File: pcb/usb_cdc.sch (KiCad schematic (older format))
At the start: 131 parts, among them J101 RS232, J102 USB, P101 I2C, P102 JATG, P103 CONN_2, P104 CONN_2, P105 CONN_2, P106 CONN_2, P107 CONN_2, Q101 BC817-40, Q102 BC817-40, Q103 MOSFET_N, Q104 MOSFET_N, Q105 MOSFET_N, Q106 MOSFET_N, Q107 MOSFET_N, Q108 MOSFET_N, Q109 MOSFET_N, Q110 MOSFET_N, Q111 MOSFET_N, Q112 MOSFET_N, Q113 MOSFET_N, Q114 MOSFET_N, Q115 MOSFET_N, Q116 MOSFET_N, Q117 MOSFET_N, Q118 MOSFET_N, U101 MAX232, U102 4001, U103 4001, U104 4001, X101 8MHz

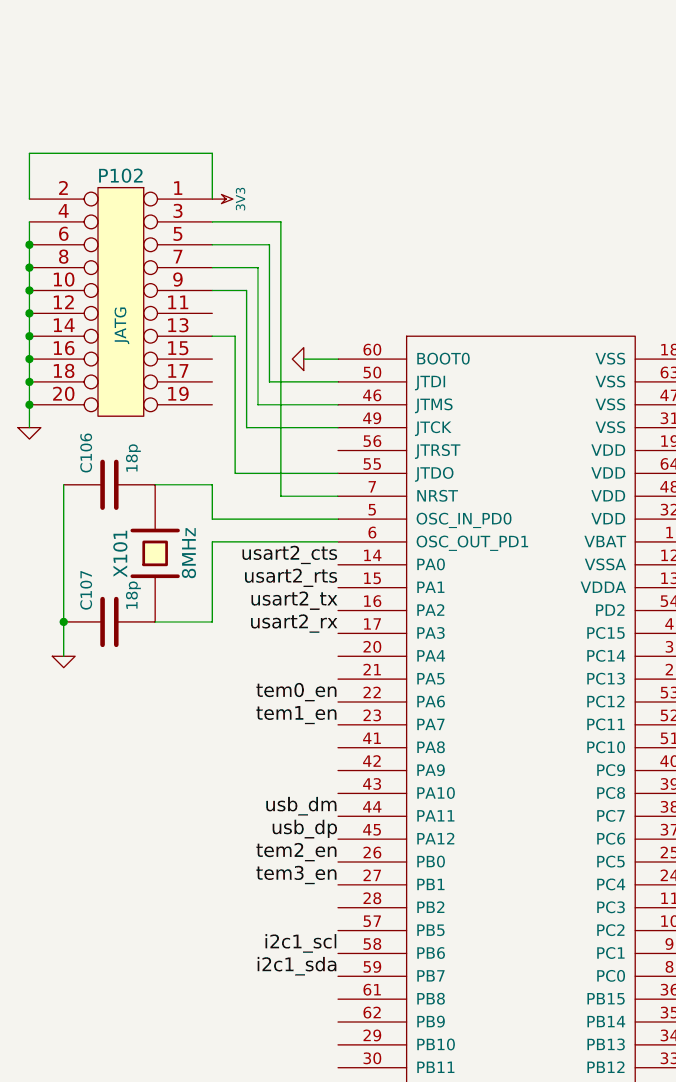
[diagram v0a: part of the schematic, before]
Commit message: implemented sensors interaction. adapt schematic for ifrmware update via uart
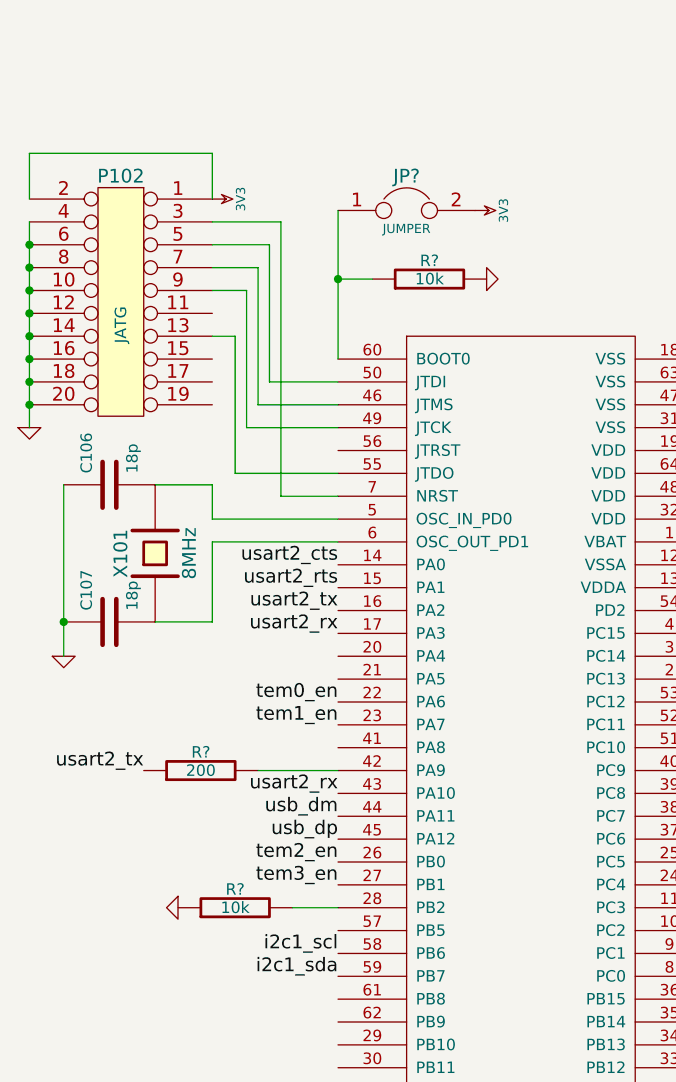
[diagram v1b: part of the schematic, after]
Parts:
- added JP?: JUMPER, symbol JUMPER
- added R? (x2): 10k, symbol R
- added R?: 200, symbol R
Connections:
- wire segments 292 -> 295
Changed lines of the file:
@@
-EESchema Schematic File Version 2  date Пнд 10 Июн 2013 18:05:02
+EESchema Schematic File Version 2  date Чтв 27 Июн 2013 16:33:48
 LIBS:power
 LIBS:device
@@
 Sheet 1 1
 Title ""
-Date "10 jun 2013"
+Date "27 jun 2013"
 Rev ""
 Comp ""
@@
 Comment4 ""
 $EndDescr
+Wire Wire Line
+	5950 4950 6300 4950
+Connection ~ 6300 2800
+Wire Wire Line
+	6450 2800 6300 2800
 Wire Notes Line
 	8000 7300 8000 7400
@@
 	8200 3550 7900 3550
 Wire Wire Line
-	6150 3150 6300 3150
-Wire Wire Line
 	5750 3950 5750 4300
 Wire Wire Line
@@
 Wire Notes Line
 	8000 8050 8000 7950
+Wire Wire Line
+	6300 3150 6300 2500
+Wire Wire Line
+	6100 5550 6300 5550
+$Comp
+L R R?
+U 1 1 51CC30F7
+P 5700 4950
+F 0 "R?" V 5780 4950 50  0000 C CNN
+F 1 "200" V 5700 4950 50  0000 C CNN
+	1    5700 4950
+	0    -1   -1   0
+$EndComp
+$Comp
+L GND #PWR?
+U 1 1 51CC2D9D
+P 5600 5550
+F 0 "#PWR?" H 5600 5550 30  0001 C CNN
+F 1 "GND" H 5600 5480 30  0001 C CNN
+	1    5600 5550
+	0    1    1    0
+$EndComp
+$Comp
+L R R?
+U 1 1 51CC2CF0
+P 5850 5550
+F 0 "R?" V 5930 5550 50  0000 C CNN
+F 1 "10k" V 5850 5550 50  0000 C CNN
+	1    5850 5550
+	0    -1   -1   0
+$EndComp
+$Comp
+L GND #PWR?
+U 1 1 51CC2CC7
+P 6950 2800
+F 0 "#PWR?" H 6950 2800 30  0001 C CNN
+F 1 "GND" H 6950 2730 30  0001 C CNN
+	1    6950 2800
+	0    -1   -1   0
+$EndComp
+$Comp
+L R R?
+U 1 1 51CC2CAD
+P 6700 2800
+F 0 "R?" V 6780 2800 50  0000 C CNN
+F 1 "10k" V 6700 2800 50  0000 C CNN
+	1    6700 2800
+	0    -1   -1   0
+$EndComp
+$Comp
+L 3V3 #PWR?
+U 1 1 51CC2C90
+P 6900 2500
+F 0 "#PWR?" H 6900 2600 40  0001 C CNN
+F 1 "3V3" H 6900 2625 40  0000 C CNN
+	1    6900 2500
+	0    1    1    0
+$EndComp
+$Comp
+L JUMPER JP?
+U 1 1 51CC2C58
+P 6600 2500
+F 0 "JP?" H 6600 2650 60  0000 C CNN
+F 1 "JUMPER" H 6600 2420 40  0000 C CNN
+	1    6600 2500
+	1    0    0    -1
+$EndComp
+Text Label 6300 5050 2    60   ~ 0
+usart2_rx
+Text Label 5450 4950 2    60   ~ 0
+usart2_tx
 Text Label 11650 11950 2    60   ~ 0
 tem3_dir
@@
 $EndComp
 $Comp
-L GND #PWR116
-U 1 1 514CAD39
-P 6150 3150
-F 0 "#PWR116" H 6150 3150 30  0001 C CNN
-F 1 "GND" H 6150 3080 30  0001 C CNN
-	1    6150 3150
-	0    1    -1   0
-$EndComp
-$Comp

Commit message: schematic: add limit switches inputs, usb led, system led, optocouplers resistors, usart2_rx protective resistor
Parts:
- added D? (x2): LED, symbol LED
- added P?: CONN_6, symbol CONN_6
- added R?: 200, symbol R
- added R? (x2): 1k, symbol R
- added R? (x8): R, symbol R
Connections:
- net labels added: ls_0, ls_1, ls_2, ls_3, ls_4
- wire segments 295 -> 306
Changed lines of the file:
@@
-EESchema Schematic File Version 2  date Чтв 27 Июн 2013 16:33:48
+EESchema Schematic File Version 2  date Втр 30 Июл 2013 22:41:59
 LIBS:power
 LIBS:device
@@
 Sheet 1 1
 Title ""
-Date "27 jun 2013"
+Date "30 jul 2013"
 Rev ""
 Comp ""
@@
 Comment4 ""
 $EndDescr
+$Comp
+L R R?
+U 1 1 51F808E6
+P 11400 12650
+F 0 "R?" V 11480 12650 50  0000 C CNN
+F 1 "R" V 11400 12650 50  0000 C CNN
+	1    11400 12650
+	0    -1   -1   0
+$EndComp
+$Comp
+L R R?
+U 1 1 51F808E1
+P 11400 11950
+F 0 "R?" V 11480 11950 50  0000 C CNN
+F 1 "R" V 11400 11950 50  0000 C CNN
+	1    11400 11950
+	0    -1   -1   0
+$EndComp
+$Comp
+L R R?
+U 1 1 51F808CA
+P 11400 10300
+F 0 "R?" V 11480 10300 50  0000 C CNN
+F 1 "R" V 11400 10300 50  0000 C CNN
+	1    11400 10300
+	0    -1   -1   0
+$EndComp
+$Comp
+L R R?
+U 1 1 51F808BE
+P 11400 9600
+F 0 "R?" V 11480 9600 50  0000 C CNN
+F 1 "R" V 11400 9600 50  0000 C CNN
+	1    11400 9600
+	0    -1   -1   0
+$EndComp
+$Comp
+L R R?
+U 1 1 51F808A7
+P 11400 7950
+F 0 "R?" V 11480 7950 50  0000 C CNN
+F 1 "R" V 11400 7950 50  0000 C CNN
+	1    11400 7950
+	0    -1   -1   0
+$EndComp
+$Comp
+L R R?
+U 1 1 51F8089B
+P 11400 7250
+F 0 "R?" V 11480 7250 50  0000 C CNN
+F 1 "R" V 11400 7250 50  0000 C CNN
+	1    11400 7250
+	0    -1   -1   0
+$EndComp
+$Comp
+L R R?
+U 1 1 51F8088A
+P 11400 5600
+F 0 "R?" V 11480 5600 50  0000 C CNN
+F 1 "R" V 11400 5600 50  0000 C CNN
+	1    11400 5600
+	0    -1   -1   0
+$EndComp
+$Comp
+L R R?
+U 1 1 51F80878
+P 11400 4900
+F 0 "R?" V 11480 4900 50  0000 C CNN
+F 1 "R" V 11400 4900 50  0000 C CNN
+	1    11400 4900
+	0    -1   -1   0
+$EndComp
+Wire Wire Line
+	9350 4650 9450 4650
+Wire Wire Line
+	9450 4650 9450 4750
+Wire Wire Line
+	5850 7600 6100 7600
+Wire Wire Line
+	5950 5050 6300 5050
 Wire Wire Line
 	5950 4950 6300 4950
@@
 Wire Wire Line
 	6100 5550 6300 5550
+Wire Wire Line
+	9300 5700 9300 5600
+Wire Wire Line
+	9300 5600 9350 5600
+Wire Wire Line
+	5350 7700 5350 7600
+Wire Wire Line
+	5350 7600 5450 7600
+Wire Wire Line
+	7900 4350 8300 4350
+Wire Wire Line
+	8300 4350 8300 4650
+Wire Wire Line
+	8300 4650 8450 4650
+$Comp
+L GND #PWR?
+U 1 1 51F80817
+P 9450 4750
+F 0 "#PWR?" H 9450 4750 30  0001 C CNN
+F 1 "GND" H 9450 4680 30  0001 C CNN
+	1    9450 4750
+	1    0    0    -1
+$EndComp
+$Comp
+L R R?
+U 1 1 51F80802
+P 8700 4650
+F 0 "R?" V 8780 4650 50  0000 C CNN
+F 1 "1k" V 8700 4650 50  0000 C CNN
+	1    8700 4650
+	0    -1   -1   0
+$EndComp
+$Comp
+L LED D?
+U 1 1 51F807B1
+P 9150 4650
+F 0 "D?" H 9150 4750 50  0000 C CNN
+F 1 "LED" H 9150 4550 50  0000 C CNN
+	1    9150 4650
+	1    0    0    -1
+$EndComp
+$Comp
+L R R?
+U 1 1 51F8075A
+P 6350 7600
+F 0 "R?" V 6430 7600 50  0000 C CNN
+F 1 "1k" V 6350 7600 50  0000 C CNN
+	1    6350 7600
+	0    -1   -1   0
+$EndComp
+$Comp
+L GND #PWR?
+U 1 1 51F8074C
+P 5350 7700
+F 0 "#PWR?" H 5350 7700 30  0001 C CNN
+F 1 "GND" H 5350 7630 30  0001 C CNN
+	1    5350 7700
+	1    0    0    -1
+$EndComp
+$Comp
+L LED D?
+U 1 1 51F8073A
+P 5650 7600
+F 0 "D?" H 5650 7700 50  0000 C CNN
+F 1 "LED" H 5650 7500 50  0000 C CNN
+	1    5650 7600
+	-1   0    0    -1
+$EndComp
+$Comp
+L R R?
+U 1 1 51F806C2
+P 5700 5050
+F 0 "R?" V 5780 5050 50  0000 C CNN
+F 1 "200" V 5700 5050 50  0000 C CNN
+	1    5700 5050
+	0    -1   -1   0
+$EndComp
+Text Label 9350 5100 2    60   ~ 0
+ls_4
+$Comp
+L CONN_6 P?
+U 1 1 51F80666
+P 9700 5350
+F 0 "P?" V 9650 5350 60  0000 C CNN
+F 1 "CONN_6" V 9750 5350 60  0000 C CNN
+	1    9700 5350
+	1    0    0    -1
+$EndComp
+Text Label 7900 5050 0    60   ~ 0
+ls_4
+Text Label 9350 5200 2    60   ~ 0
+ls_3
+Text Label 9350 5300 2    60   ~ 0
+ls_2
+Text Label 9350 5400 2    60   ~ 0
+ls_1
+Text Label 9350 5500 2    60   ~ 0
+ls_0
+$Comp
+L GND #PWR?
+U 1 1 51F8058D
+P 9300 5700
+F 0 "#PWR?" H 9300 5700 30  0001 C CNN
+F 1 "GND" H 9300 5630 30  0001 C CNN
+	1    9300 5700
+	1    0    0    -1
+$EndComp
+Text Label 7900 5250 0    60   ~ 0
+ls_3
+Text Label 7900 5450 0    60   ~ 0
+ls_2
+Text Label 7900 5650 0    60   ~ 0
+ls_1
+Text Label 7900 5850 0    60   ~ 0
+ls_0
 $Comp
 L R R?
@@
 	1    0    0    -1
 $EndComp
-Text Label 6300 5050 2    60   ~ 0
+Text Label 5450 5050 2    60   ~ 0
 usart2_rx
 Text Label 5450 4950 2    60   ~ 0
 usart2_tx
-Text Label 11650 11950 2    60   ~ 0
+Text Label 11150 11950 2    60   ~ 0
 tem3_dir
-Text Label 11650 12650 2    60   ~ 0
+Text Label 11150 12650 2    60   ~ 0
 tem3_en
-Text Label 11650 9600 2    60   ~ 0
+Text Label 11150 9600 2    60   ~ 0
 tem2_dir
-Text Label 11650 10300 2    60   ~ 0
+Text Label 11150 10300 2    60   ~ 0
 tem2_en
-Text Label 11650 7250 2    60   ~ 0
+Text Label 11150 7250 2    60   ~ 0
 tem1_dir
-Text Label 11650 7950 2    60   ~ 0
+Text Label 11150 7950 2    60   ~ 0
 tem1_en
-Text Label 11650 5600 2    60   ~ 0
+Text Label 11150 5600 2    60   ~ 0
 tem0_en
-Text Label 11650 4900 2    60   ~ 0
+Text Label 11150 4900 2    60   ~ 0
 tem0_dir
 $Comp

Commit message: schematic: moar LEDs
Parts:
- removed P?: CONN_6, symbol CONN_6
- added D? (x4): LED, symbol LED
- added P?: CONN_5X2, symbol CONN_5X2
- added R? (x4): 1k, symbol R
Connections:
- wire segments 306 -> 313
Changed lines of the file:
@@
-EESchema Schematic File Version 2  date Втр 30 Июл 2013 22:41:59
+EESchema Schematic File Version 2  date Срд 31 Июл 2013 16:10:16
 LIBS:power
 LIBS:device
@@
 Sheet 1 1
 Title ""
-Date "30 jul 2013"
+Date "31 jul 2013"
 Rev ""
 Comp ""
@@
 Comment4 ""
 $EndDescr
-$Comp
-L R R?
-U 1 1 51F808E6
-P 11400 12650
-F 0 "R?" V 11480 12650 50  0000 C CNN
-F 1 "R" V 11400 12650 50  0000 C CNN
-	1    11400 12650
-	0    -1   -1   0
-$EndComp
-$Comp
-L R R?
-U 1 1 51F808E1
-P 11400 11950
-F 0 "R?" V 11480 11950 50  0000 C CNN
-F 1 "R" V 11400 11950 50  0000 C CNN
-	1    11400 11950
-	0    -1   -1   0
-$EndComp
-$Comp
-L R R?
-U 1 1 51F808CA
-P 11400 10300
-F 0 "R?" V 11480 10300 50  0000 C CNN
-F 1 "R" V 11400 10300 50  0000 C CNN
-	1    11400 10300
-	0    -1   -1   0
-$EndComp
-$Comp
-L R R?
-U 1 1 51F808BE
-P 11400 9600
-F 0 "R?" V 11480 9600 50  0000 C CNN
-F 1 "R" V 11400 9600 50  0000 C CNN
-	1    11400 9600
-	0    -1   -1   0
-$EndComp
-$Comp
-L R R?
-U 1 1 51F808A7
-P 11400 7950
-F 0 "R?" V 11480 7950 50  0000 C CNN
-F 1 "R" V 11400 7950 50  0000 C CNN
-	1    11400 7950
-	0    -1   -1   0
-$EndComp
-$Comp
-L R R?
-U 1 1 51F8089B
-P 11400 7250
-F 0 "R?" V 11480 7250 50  0000 C CNN
-F 1 "R" V 11400 7250 50  0000 C CNN
-	1    11400 7250
-	0    -1   -1   0
-$EndComp
-$Comp
-L R R?
-U 1 1 51F8088A
-P 11400 5600
-F 0 "R?" V 11480 5600 50  0000 C CNN
-F 1 "R" V 11400 5600 50  0000 C CNN
-	1    11400 5600
-	0    -1   -1   0
-$EndComp
-$Comp
-L R R?
-U 1 1 51F80878
-P 11400 4900
-F 0 "R?" V 11480 4900 50  0000 C CNN
-F 1 "R" V 11400 4900 50  0000 C CNN
-	1    11400 4900
-	0    -1   -1   0
-$EndComp
+Wire Wire Line
+	11150 7650 11150 7950
+Wire Wire Line
+	11150 12300 11150 12650
+Wire Wire Line
+	10250 7600 10250 7650
+Wire Wire Line
+	10250 5200 10250 5250
+Connection ~ 10150 5400
+Connection ~ 10150 5200
 Wire Wire Line
 	9350 4650 9450 4650
@@
 	15800 6300 15600 6300
 Wire Wire Line
-	15800 5100 15800 5800
+	15800 5800 15800 5100
 Wire Wire Line
 	15600 5800 15600 5700
@@
 Connection ~ 17600 6100
 Wire Wire Line
-	17600 5900 17600 6100
+	17600 6100 17600 5900
 Connection ~ 18550 6100
 Wire Wire Line
@@
 Connection ~ 18550 5500
 Wire Wire Line
-	18550 5500 18550 5300
-Wire Wire Line
-	17600 5500 17600 5300
+	18550 5300 18550 5500
+Wire Wire Line
+	17600 5300 17600 5500
 Wire Wire Line
 	18350 6100 18350 5900
 Connection ~ 18350 6100
 Wire Wire Line
-	17400 6100 17400 5900
+	17400 5900 17400 6100
 Connection ~ 17400 6100
 Connection ~ 19250 5700
@@
 Connection ~ 18350 7850
 Wire Wire Line
-	18350 7650 18350 7850
+	18350 7850 18350 7650
 Wire Wire Line
 	19250 8450 16700 8450
 Wire Wire Line
-	18550 8250 18550 8450
+	18550 8450 18550 8250
 Connection ~ 18550 8450
 Wire Wire Line
-	17600 8250 17600 8450
+	17600 8450 17600 8250
 Connection ~ 17600 8450
 Connection ~ 16700 7450
@@
 	15600 8050 15600 8150
 Wire Wire Line
-	15800 7450 15800 8150
+	15800 8150 15800 7450
 Wire Wire Line
 	15800 8650 15600 8650
@@
 	15800 13350 15600 13350
 Wire Wire Line
-	15800 12150 15800 12850
+	15800 12850 15800 12150
 Wire Wire Line
 	15600 12850 15600 12750
@@
 Connection ~ 17600 13150
 Wire Wire Line
-	17600 12950 17600 13150
+	17600 13150 17600 12950
 Connection ~ 18550 13150
 Wire Wire Line
@@
 Connection ~ 18550 12550
 Wire Wire Line
-	18550 12550 18550 12350
-Wire Wire Line
-	17600 12550 17600 12350
+	18550 12350 18550 12550
+Wire Wire Line
+	17600 12350 17600 12550
 Wire Wire Line
 	18350 13150 18350 12950
 Connection ~ 18350 13150
 Wire Wire Line
-	17400 13150 17400 12950
+	17400 12950 17400 13150
 Connection ~ 17400 13150
 Connection ~ 19250 12750
@@
 Connection ~ 18350 10200
 Wire Wire Line
-	18350 10000 18350 10200
+	18350 10200 18350 10000
 Wire Wire Line
 	19250 10800 16700 10800
 Wire Wire Line
-	18550 10600 18550 10800
+	18550 10800 18550 10600
 Connection ~ 18550 10800
 Wire Wire Line
-	17600 10600 17600 10800
+	17600 10800 17600 10600
 Connection ~ 17600 10800
 Connection ~ 16700 9800
@@
 	15600 10400 15600 10500
 Wire Wire Line
-	15800 9800 15800 10500
+	15800 10500 15800 9800
 Wire Wire Line
 	15800 11000 15600 11000
@@
 	11650 10700 11650 10800
 Wire Wire Line
-	17400 12350 17400 12550
-Wire Wire Line
-	17400 7650 17400 7850
+	17400 12550 17400 12350
+Wire Wire Line
+	17400 7850 17400 7650
 Wire Wire Line
 	15750 1800 15750 2000
@@
 	6100 5550 6300 5550
 Wire Wire Line
-	9300 5700 9300 5600
-Wire Wire Line
-	9300 5600 9350 5600
-Wire Wire Line
 	5350 7700 5350 7600
 Wire Wire Line
@@
 Wire Wire Line
 	8300 4650 8450 4650
+Connection ~ 10150 5300
+Wire Wire Line
+	10150 5100 10150 5650
+Connection ~ 10150 5500
+Wire Wire Line
+	11150 5250 11150 5600
+Wire Wire Line
+	10250 9900 10250 9950
+Wire Wire Line
+	10250 12250 10250 12300
+Wire Wire Line
+	11150 9950 11150 10300
+$Comp
+L LED D?
+U 1 1 51F8FE8A
+P 10950 12300
+F 0 "D?" H 10950 12400 50  0000 C CNN
+F 1 "LED" H 10950 12200 50  0000 C CNN
+	1    10950 12300
+	1    0    0    -1
+$EndComp
+$Comp
+L R R?
+U 1 1 51F8FE89
+P 10500 12300
+F 0 "R?" V 10580 12300 50  0000 C CNN
+F 1 "1k" V 10500 12300 50  0000 C CNN
+	1    10500 12300
+	0    -1   -1   0
+$EndComp
+$Comp
+L 3V3 #PWR?
+U 1 1 51F8FE88
+P 10250 12250
+F 0 "#PWR?" H 10250 12350 40  0001 C CNN
+F 1 "3V3" H 10250 12375 40  0000 C CNN
+	1    10250 12250
+	1    0    0    -1
+$EndComp
+$Comp
+L 3V3 #PWR?
+U 1 1 51F8FE7E
+P 10250 9900
+F 0 "#PWR?" H 10250 10000 40  0001 C CNN
+F 1 "3V3" H 10250 10025 40  0000 C CNN
+	1    10250 9900
+	1    0    0    -1
+$EndComp
+$Comp
+L R R?
+U 1 1 51F8FE7D
+P 10500 9950
+F 0 "R?" V 10580 9950 50  0000 C CNN
+F 1 "1k" V 10500 9950 50  0000 C CNN
+	1    10500 9950
+	0    -1   -1   0
+$EndComp
+$Comp
+L LED D?
+U 1 1 51F8FE7C
+P 10950 9950
+F 0 "D?" H 10950 10050 50  0000 C CNN
+F 1 "LED" H 10950 9850 50  0000 C CNN
+	1    10950 9950
+	1    0    0    -1
+$EndComp
+$Comp
+L LED D?
+U 1 1 51F8FE59
+P 10950 7650
+F 0 "D?" H 10950 7750 50  0000 C CNN
+F 1 "LED" H 10950 7550 50  0000 C CNN
+	1    10950 7650
+	1    0    0    -1
+$EndComp
+$Comp
+L R R?
+U 1 1 51F8FE58
+P 10500 7650
+F 0 "R?" V 10580 7650 50  0000 C CNN
+F 1 "1k" V 10500 7650 50  0000 C CNN
+	1    10500 7650
+	0    -1   -1   0
+$EndComp
+$Comp
+L 3V3 #PWR?
+U 1 1 51F8FE57
+P 10250 7600
+F 0 "#PWR?" H 10250 7700 40  0001 C CNN
+F 1 "3V3" H 10250 7725 40  0000 C CNN
+	1    10250 7600
+	1    0    0    -1
+$EndComp
+$Comp
+L 3V3 #PWR?
+U 1 1 51F8FE02
+P 10250 5200
+F 0 "#PWR?" H 10250 5300 40  0001 C CNN
+F 1 "3V3" H 10250 5325 40  0000 C CNN
+	1    10250 5200
+	1    0    0    -1
+$EndComp
+$Comp
+L R R?
+U 1 1 51F8FDE6
+P 10500 5250
+F 0 "R?" V 10580 5250 50  0000 C CNN
+F 1 "1k" V 10500 5250 50  0000 C CNN
+	1    10500 5250
+	0    -1   -1   0
+$EndComp
+$Comp
+L LED D?
+U 1 1 51F8FD3C
+P 10950 5250
+F 0 "D?" H 10950 5350 50  0000 C CNN
+F 1 "LED" H 10950 5150 50  0000 C CNN
+	1    10950 5250
+	1    0    0    -1
+$EndComp
+$Comp
+L CONN_5X2 P?
+U 1 1 51F8FC65
+P 9750 5300
+F 0 "P?" H 9750 5600 60  0000 C CNN
+F 1 "CONN_5X2" V 9750 5300 50  0000 C CNN
+	1    9750 5300
+	1    0    0    -1
+$EndComp
+$Comp
+L R R?
+U 1 1 51F808E6
+P 11400 12650
+F 0 "R?" V 11480 12650 50  0000 C CNN
+F 1 "R" V 11400 12650 50  0000 C CNN
+	1    11400 12650
+	0    -1   -1   0
+$EndComp
+$Comp
+L R R?
+U 1 1 51F808E1
+P 11400 11950
+F 0 "R?" V 11480 11950 50  0000 C CNN
+F 1 "R" V 11400 11950 50  0000 C CNN
+	1    11400 11950
+	0    -1   -1   0
+$EndComp
+$Comp
+L R R?
+U 1 1 51F808CA
+P 11400 10300
+F 0 "R?" V 11480 10300 50  0000 C CNN
+F 1 "R" V 11400 10300 50  0000 C CNN
+	1    11400 10300
+	0    -1   -1   0
+$EndComp
+$Comp
+L R R?
+U 1 1 51F808BE
+P 11400 9600
+F 0 "R?" V 11480 9600 50  0000 C CNN
+F 1 "R" V 11400 9600 50  0000 C CNN
+	1    11400 9600
+	0    -1   -1   0
+$EndComp
+$Comp
+L R R?
+U 1 1 51F808A7
+P 11400 7950
+F 0 "R?" V 11480 7950 50  0000 C CNN
+F 1 "R" V 11400 7950 50  0000 C CNN
+	1    11400 7950
+	0    -1   -1   0
+$EndComp
+$Comp
+L R R?
+U 1 1 51F8089B
+P 11400 7250
+F 0 "R?" V 11480 7250 50  0000 C CNN
+F 1 "R" V 11400 7250 50  0000 C CNN
+	1    11400 7250
+	0    -1   -1   0
+$EndComp
+$Comp
+L R R?
+U 1 1 51F8088A
+P 11400 5600
+F 0 "R?" V 11480 5600 50  0000 C CNN
+F 1 "R" V 11400 5600 50  0000 C CNN
+	1    11400 5600
+	0    -1   -1   0
+$EndComp
+$Comp
+L R R?
+U 1 1 51F80878
+P 11400 4900
+F 0 "R?" V 11480 4900 50  0000 C CNN
+F 1 "R" V 11400 4900 50  0000 C CNN
+	1    11400 4900
+	0    -1   -1   0
+$EndComp
 $Comp
 L GND #PWR?
@@
 Text Label 9350 5100 2    60   ~ 0
 ls_4
-$Comp
-L CONN_6 P?
-U 1 1 51F80666
-P 9700 5350
-F 0 "P?" V 9650 5350 60  0000 C CNN
-F 1 "CONN_6" V 9750 5350 60  0000 C CNN
-	1    9700 5350
-	1    0    0    -1
-$EndComp
 Text Label 7900 5050 0    60   ~ 0
 ls_4
@@
 L GND #PWR?
 U 1 1 51F8058D
-P 9300 5700
-F 0 "#PWR?" H 9300 5700 30  0001 C CNN
-F 1 "GND" H 9300 5630 30  0001 C CNN
-	1    9300 5700
-	1    0    0    -1
-$EndComp
+P 10150 5650
+F 0 "#PWR?" H 10150 5650 30  0001 C CNN
+F 1 "GND" H 10150 5580 30  0001 C CNN
+	1    10150 5650
+	1    0    0    -1
+$EndComp

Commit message: Added PCB desing
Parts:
- removed C120, C121, C122, C123: C, symbol C
- removed D103, D104, D105, D106, D107, D108, D109, D110: TLP181GB, symbol TLP181GB
- removed D111, D112, D113, D114, D115, D116, D117, D118, D135, D136, D137, D138, D139, D140, D141, D142: ZENER, symbol ZENER
- removed D119, D120, D121, D122, D123, D124, D125, D126, D127, D128, D129, D130, D131, D132, D133, D134: DIODE, symbol DIODE
- removed D? (x4): LED, symbol LED
- removed P103, P104, P105, P106, P107: CONN_2, symbol CONN_2
- removed Q103, Q104, Q105, Q106, Q107, Q108, Q109, Q110, Q111, Q112, Q113, Q114, Q115, Q116, Q117, Q118: MOSFET_N, symbol MOSFET_N
- removed R110, R111, R112, R113, R114, R115, R116, R117, R? (x8): R, symbol R
- removed R118, R119, R120, R121, R122, R123, R124, R125: 10k, symbol R
- removed R126, R127, R128, R129, R130, R131, R132, R133: 2k, symbol R
- removed R? (x4): 1k, symbol R
- removed U102, U103, U104: 4001, symbol 4001
- added C22, C23, C24: C, symbol C
- added C3: 0.1, symbol C
- added C7: 10.0, symbol C
- added D12, D13, D14, D15, D16, D17, D18, D19: TLP181GB, symbol TLP181GB
- added D2: LD1117DT33CTR, symbol LD1117
- added D20, D21, D22, D23, D24, D25, D26, D27, D7: LED, symbol LED
- added D5: USBLC6, ~, symbol USBLC6
- added P3: CONN_4, symbol CONN_4
- added P5, P6, P7, P8: CONN_2, symbol CONN_2
- added Q10, Q11, Q12, Q13, Q14, Q15, Q16, Q17, Q18, Q3, Q4, Q5, Q6, Q7, Q8, Q9: IRLBD59N04E, symbol IRLBD59N04E
- added R14, R21, R22, R23, R24, R25, R26, R27, R28, R29, R30, R31, R32, R33, R34, R35, R36, R41, R42, R43, R44, R49, R50, R51, R52: R, symbol R
- added R37, R38, R39, R40, R45, R46, R47, R48: 10k, symbol R
- added R53, R54, R55, R56, R57, R58, R59, R60: 2k, symbol R
- added U2, U3, U4: 4001, symbol 4001
- gave numbers to parts that had none: 10
- renumbered C106 to C1, C104 to C10, C105 to C11, C117 to C12, C109 to C13, C110 to C14, C118 to C15, C111 to C16, C112 to C17, C119 to C18, C113 to C19, C107 to C2, C114 to C20, C115 to C21, C101 to C4, C102 to C5, C103 to C6, C116 to C8, C108 to C9, D101 to D3, D102 to D4, F101 to F1, J101 to J1, J102 to J2, P101 to P1, P102 to P2, Q101 to Q1, Q102 to Q2, R106 to R10, R107 to R12, R108 to R15, R109 to R16, R101 to R3, R102 to R5, R103 to R6, R104 to R7, R105 to R9, U101 to U1, X101 to X1
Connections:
- wire segments 313 -> 324
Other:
- note added: "12 V POWER ON"
- note added: "HOT"
- note added: "ICE"
- note added: "LINK"
- note added: "USB POWER"
- note removed: "U\nS\nB\nL\nC\n6"
- moved on the sheet: C1, C10, C11, C12, C13, C14, C15, C16, C17, C18, C19, C2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
